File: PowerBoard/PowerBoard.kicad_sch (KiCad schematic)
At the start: 166 parts, among them IC101 LM340, IC102 7905, IC401 LM379, IC501 LM555xM, J103 Conn_01x02, J107 Conn_01x02, J204 Conn_01x04, J401 Conn_01x04, J402 Conn_01x04, J506 Conn_01x02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

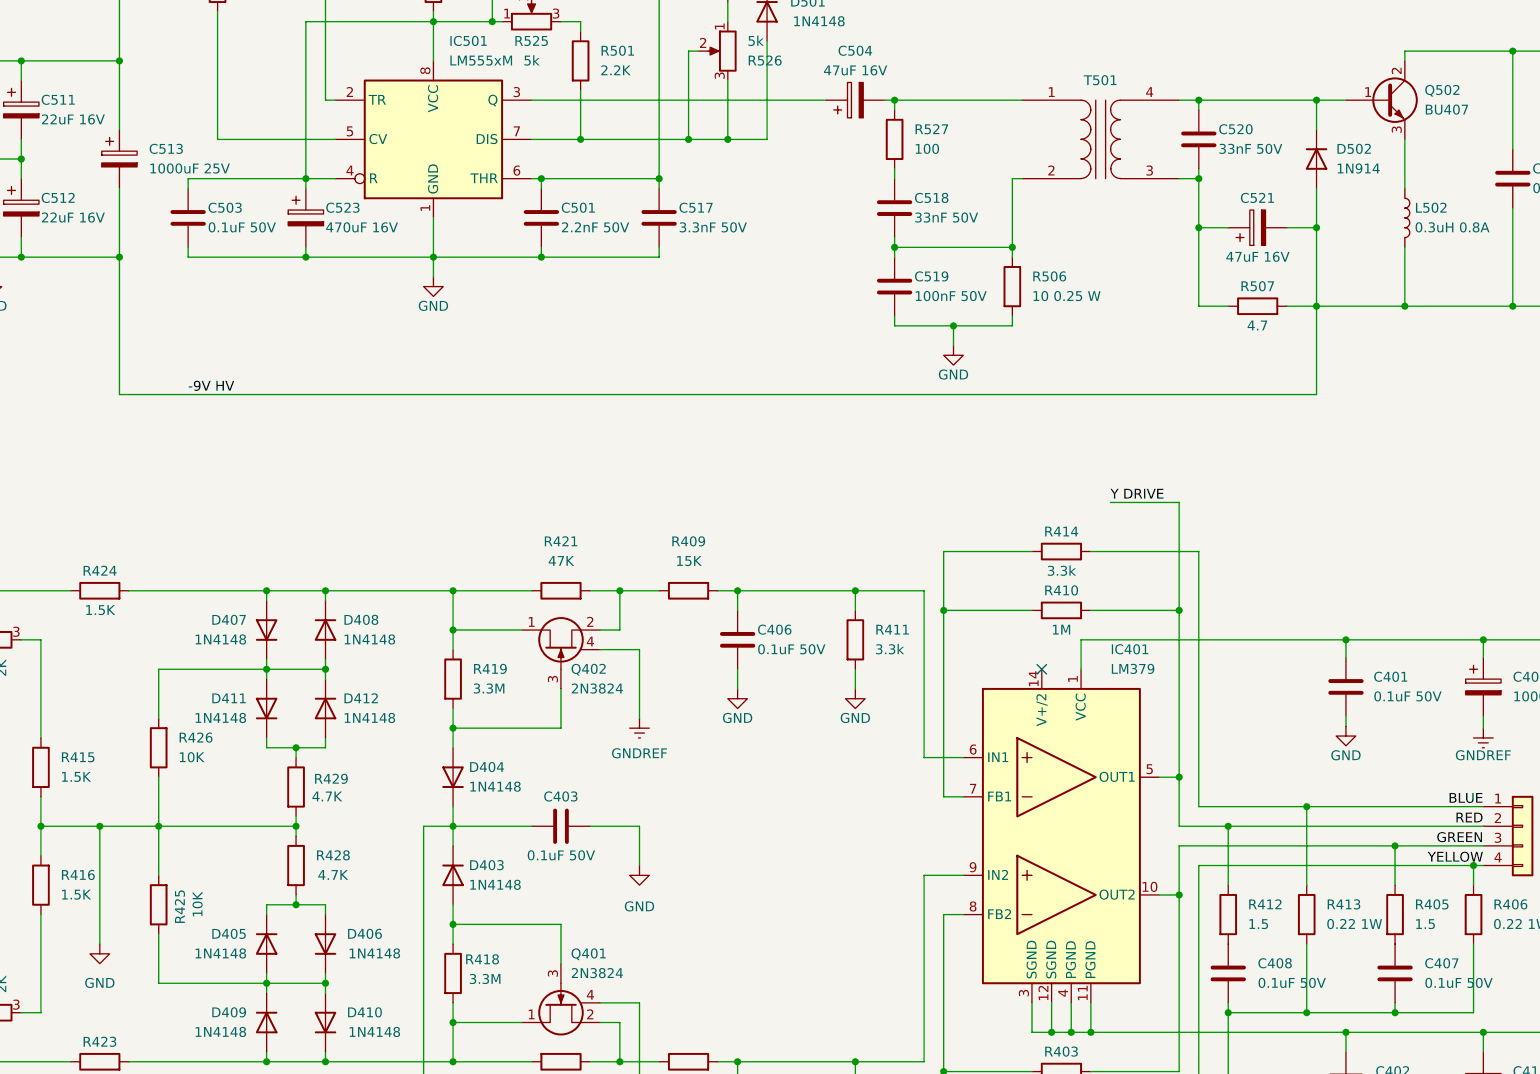
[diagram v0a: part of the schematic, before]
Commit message: Minor location adjustment
Minor location adjustment for better readability
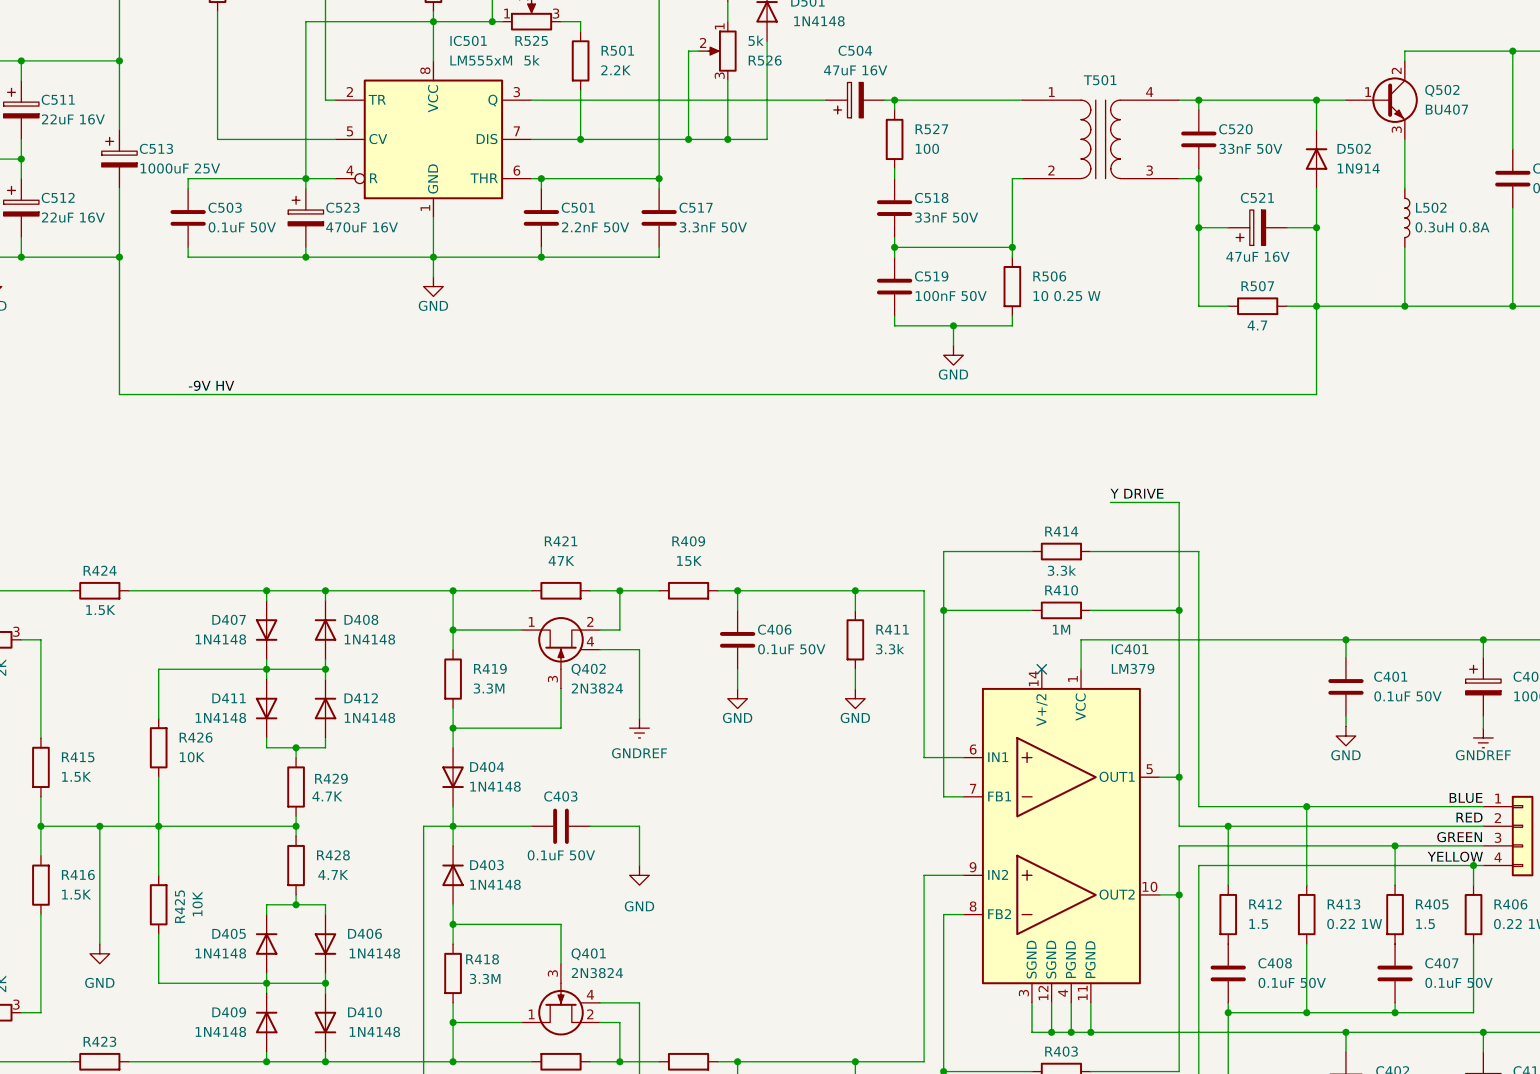
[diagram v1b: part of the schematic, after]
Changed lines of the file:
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@@
   (symbol (lib_id "Device:C_Polarized") (at 68.58 69.85 0) (unit 1)
     (in_bom yes) (on_board yes)
-    (property "Reference" "C513" (id 0) (at 72.39 68.58 0)
-      (effects (font (size 1.27 1.27)) (justify left))
-    )
-    (property "Value" "1000uF 25V" (id 1) (at 72.39 71.12 0)
+    (property "Reference" "C513" (id 0) (at 71.12 68.58 0)
+      (effects (font (size 1.27 1.27)) (justify left))
+    )
+    (property "Value" "1000uF 25V" (id 1) (at 71.12 71.12 0)
       (effects (font (size 1.27 1.27)) (justify left))
     )
@@
   )
   (symbol (lib_id "Device:R") (at 222.25 167.64 0) (unit 1)
-    (in_bom yes) (on_board yes) (fields_autoplaced)
+    (in_bom yes) (on_board yes)
     (property "Reference" "R413" (id 0) (at 224.79 166.3699 0)
       (effects (font (size 1.27 1.27)) (justify left))
     )
-    (property "Value" "0.22 1W" (id 1) (at 224.79 168.9099 0)
-      (effects (font (size 1.27 1.27)) (justify left))
-    )
+    (property "Value" "0.22 1W" (id 1) (at 224.79 168.91 0)
+      (effects (font (size 1.27 1.27)) (justify left))
+    )

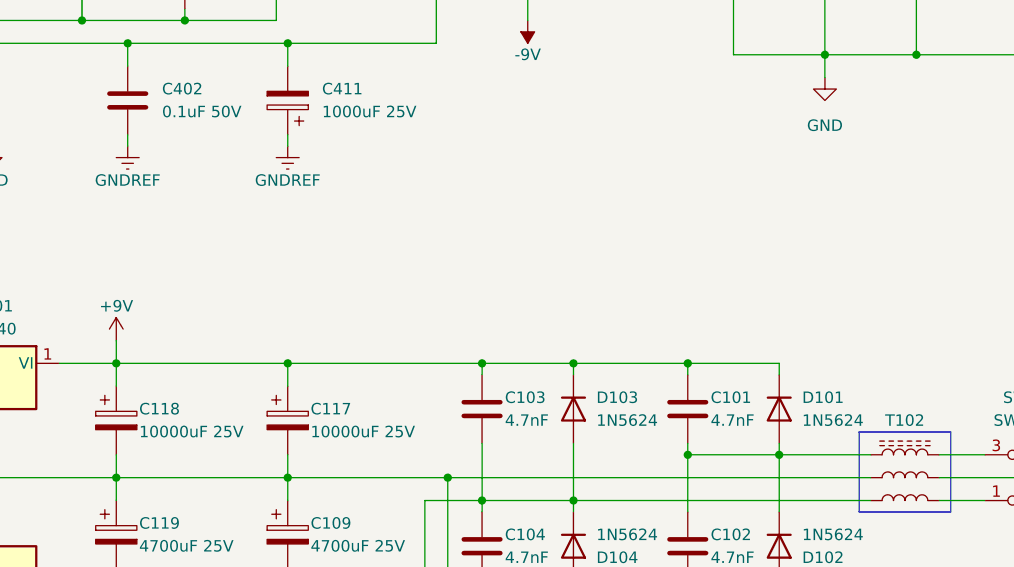
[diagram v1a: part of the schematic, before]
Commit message: Added a comment about the 9V voltage which is not 9V...
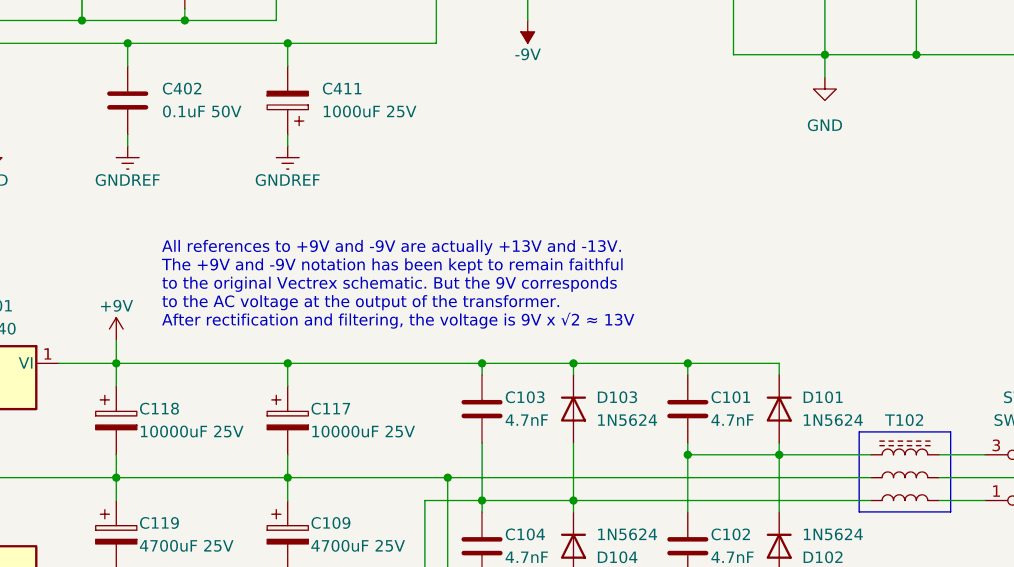
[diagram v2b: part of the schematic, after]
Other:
- note added: "All references to +9V and -9V are actually +13V and -13V. The +9V and -9V notation has been kept to remain faithful to the original Vectrex schematic. But the 9V corresponds to the AC voltage at the output of the transformer. After rectification and filtering, the voltage is 9V x √2 ≈ 13V"
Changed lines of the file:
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@@
     (stroke (width 0) (type default) (color 0 0 0 0))
+  )
+  (text "All references to +9V and -9V are actually +13V and -13V.\nThe +9V and -9V notation has been kept to remain faithful\nto the original Vectrex schematic. But the 9V corresponds\nto the AC voltage at the output of the transformer.\nAfter rectification and filtering, the voltage is 9V x √2 ≈ 13V"
+    (at 231.14 214.63 0)
+    (effects (font (size 1.27 1.27)) (justify left bottom))
   )
   (label "RED" (at 245.11 156.21 180)

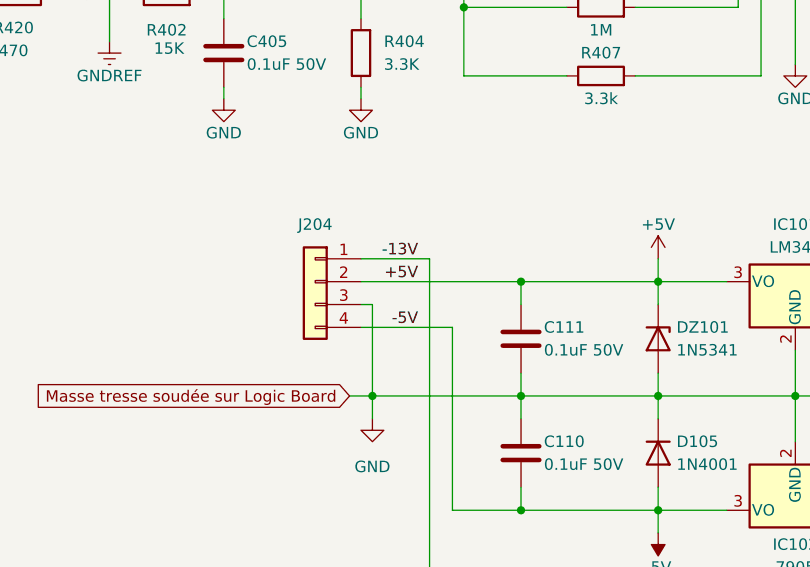
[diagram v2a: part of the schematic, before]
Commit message: Rename -13V to -13VREF
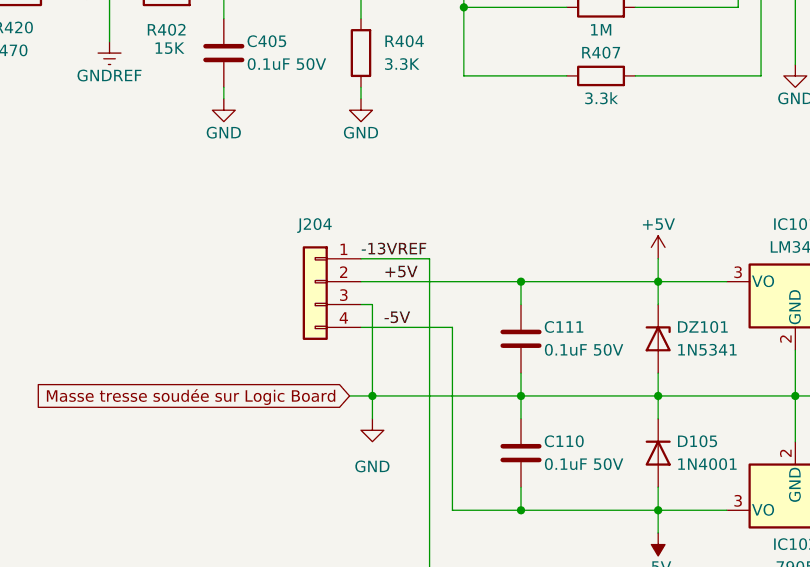
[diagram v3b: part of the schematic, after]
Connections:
- net -13V renamed -13VREF
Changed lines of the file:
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@@
     (effects (font (size 1.27 1.27)) (justify left bottom))
   )
-  (label "+5V" (at 170.18 218.44 180)
-    (effects (font (size 1.27 1.27)) (justify right bottom))
+  (label "+5V" (at 166.37 218.44 0)
+    (effects (font (size 1.27 1.27)) (justify left bottom))
   )
   (label "Y DRIVE" (at 48.26 198.12 180)
@@
     (effects (font (size 1.27 1.27)) (justify left bottom))
   )
-  (label "-5V" (at 170.18 223.52 180)
-    (effects (font (size 1.27 1.27)) (justify right bottom))
+  (label "-5V" (at 166.37 223.52 0)
+    (effects (font (size 1.27 1.27)) (justify left bottom))
   )
   (label "GREEN" (at 378.46 54.61 0)
@@
     (effects (font (size 1.27 1.27)) (justify left bottom))
   )
-  (label "-13V" (at 170.18 215.9 180)
-    (effects (font (size 1.27 1.27)) (justify right bottom))
+  (label "-13VREF" (at 163.83 215.9 0)
+    (effects (font (size 1.27 1.27)) (justify left bottom))
   )
   (label "X Axis" (at 34.29 157.48 0)
